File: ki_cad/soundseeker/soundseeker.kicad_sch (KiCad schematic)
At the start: 0 parts

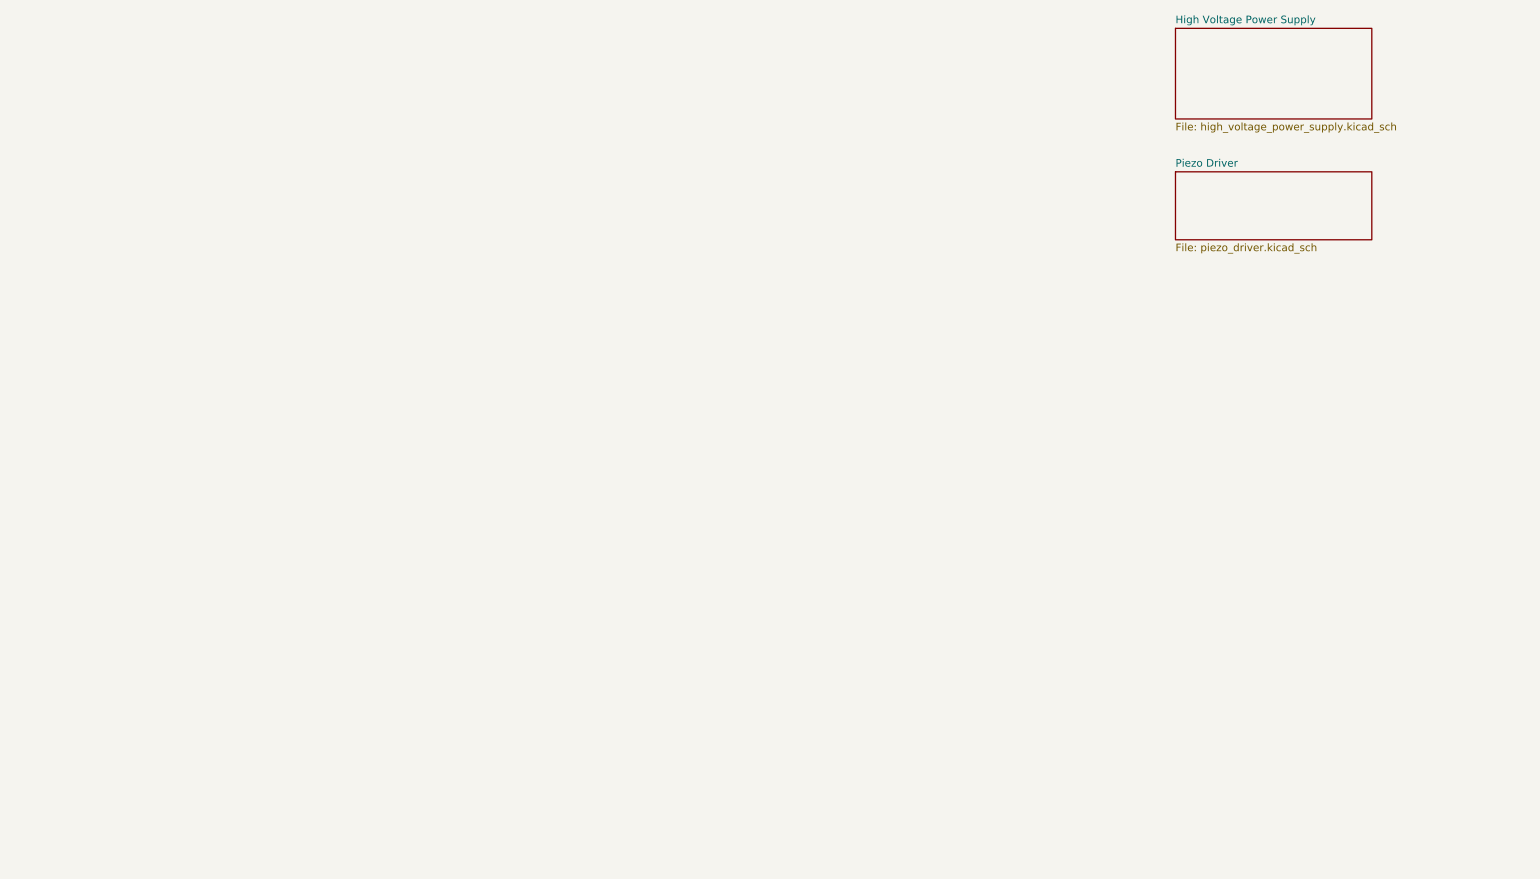
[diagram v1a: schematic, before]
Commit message: add preamp schematic
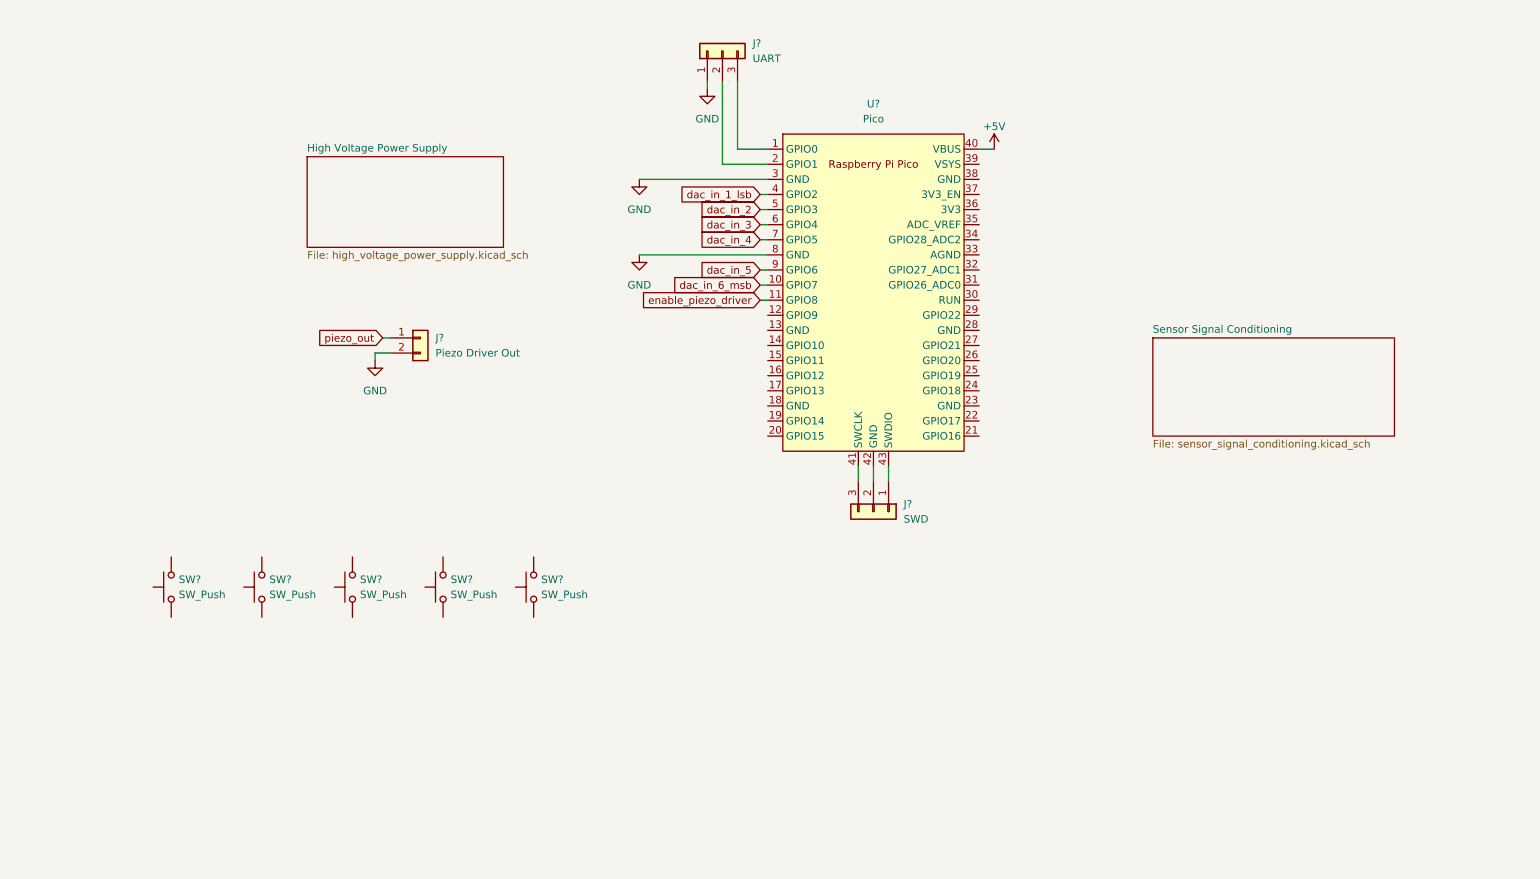
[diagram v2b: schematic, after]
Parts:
- added J?: SWD, symbol Connector_Generic:Conn_01x03
- added J?: Piezo Driver Out, symbol Connector_Generic:Conn_01x02
- added J?: UART, symbol Connector_Generic:Conn_01x03
- added SW? (x5): SW_Push, symbol Switch:SW_Push
- added U?: Pico, RPi_Pico:RPi_Pico_SMD_TH, symbol MCU_RaspberryPi_and_Boards:Pico
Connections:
- new net: J?.1 (Pin_1), U?.43 (SWDIO)
- new net: J?.2 (Pin_2), U?.42 (GND)
- new net: J?.3 (Pin_3), U?.41 (SWCLK)
- new net: J?.2 (Pin_2), U?.2 (GPIO1)
- new net: J?.3 (Pin_3), U?.1 (GPIO0)
- new net +5V: U?.40 (VBUS)
- new net GND: J?.1 (Pin_1), J?.2 (Pin_2), U?.3 (GND), U?.8 (GND)
- new net dac_in_1_lsb: U?.4 (GPIO2)
- new net dac_in_2: U?.5 (GPIO3)
- new net dac_in_3: U?.6 (GPIO4)
- new net dac_in_4: U?.7 (GPIO5)
- new net dac_in_5: U?.9 (GPIO6)
- new net dac_in_6_msb: U?.10 (GPIO7)
- new net enable_piezo_driver: U?.11 (GPIO8)
- new net piezo_out: J?.1 (Pin_1)
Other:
- removed sheet Piezo Driver
- added sheet Sensor Signal Conditioning (sensor_signal_conditioning.kicad_sch)

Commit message: schematic
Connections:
- net GND: now also U?.13 (GND), U?.18 (GND), U?.23 (GND), U?.28 (GND), U?.38 (GND)
- net ADC_DOUT: now reaches U?.21 (GPIO16)
- net ADC_CS: now reaches U?.22 (GPIO17)
- net ADC_SLCK: now reaches U?.24 (GPIO18)
- net enable_analog_power_supply: now reaches U?.26 (GPIO20)

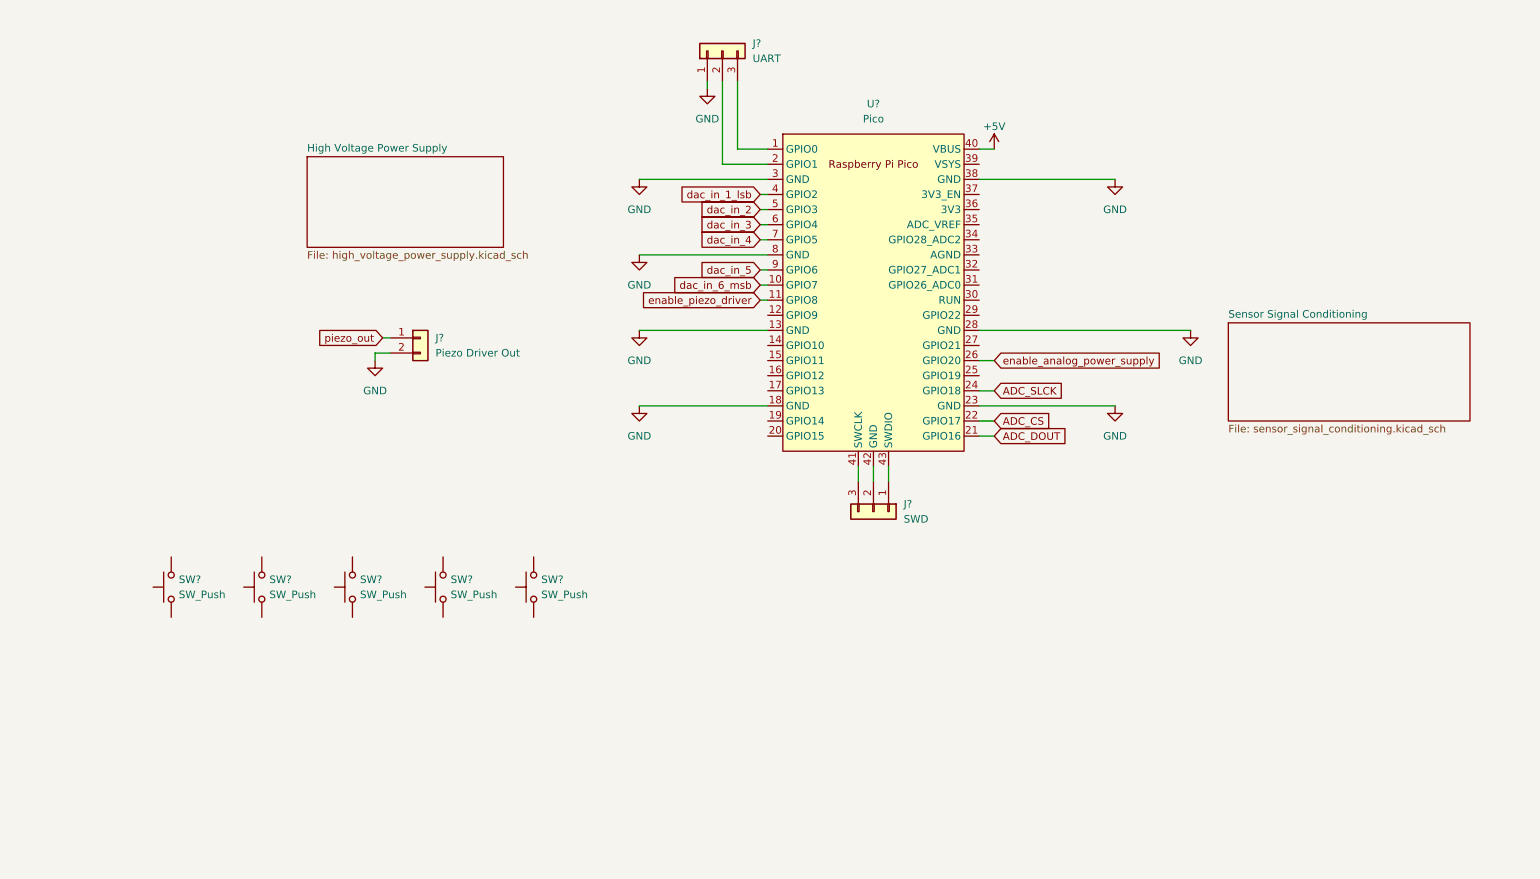
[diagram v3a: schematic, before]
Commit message: add buttons and display spi connections
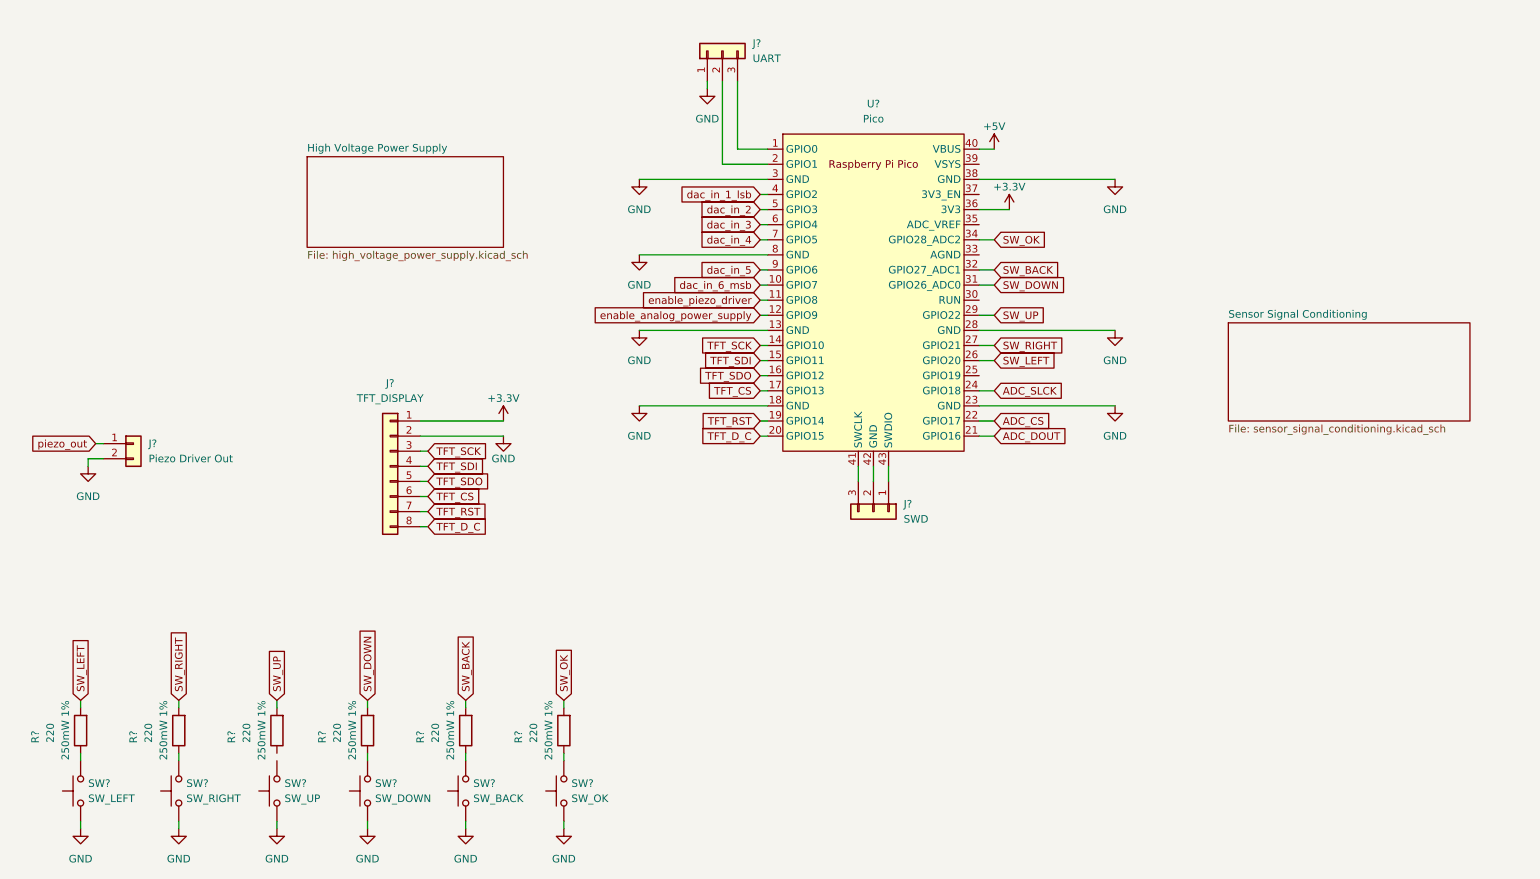
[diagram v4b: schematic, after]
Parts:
- removed SW?: SW_Push, symbol Switch:SW_Push
- added J?: TFT_DISPLAY, symbol Connector_Generic:Conn_01x08
- added R? (x6): 220, Resistor_SMD:R_0805_2012Metric_Pad1.20x1.40mm_HandSolder, symbol Device:R
- added SW?: SW_BACK, symbol Switch:SW_Push
- added SW?: SW_OK, symbol Switch:SW_Push
- SW?: value SW_Push -> SW_DOWN
- SW?: value SW_Push -> SW_RIGHT
- SW?: value SW_Push -> SW_LEFT
- SW?: value SW_Push -> SW_UP
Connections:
- net GND: now also SW?.1, SW?.1, SW?.1, SW?.1, J?.2 (Pin_2), SW?.1, SW?.1
- net enable_analog_power_supply: now also U?.12 (GPIO9); no longer U?.26 (GPIO20)
- net at SW?.2: now also R?.1 (x3)
- net TFT_SCK: now reaches U?.14 (GPIO10)
- net TFT_SCK: now also J?.3 (Pin_3)
- net TFT_SDI: now reaches U?.15 (GPIO11)
- net TFT_SDI: now also J?.4 (Pin_4)
- net TFT_SDO: now reaches U?.16 (GPIO12)
- net TFT_SDO: now also J?.5 (Pin_5)
- net TFT_CS: now reaches U?.17 (GPIO13)
- net TFT_CS: now also J?.6 (Pin_6)
- net TFT_RST: now reaches U?.19 (GPIO14)
- net TFT_RST: now also J?.7 (Pin_7)
- net TFT_D_C: now reaches U?.20 (GPIO15)
- net TFT_D_C: now also J?.8 (Pin_8)
- net SW_RIGHT: now reaches U?.27 (GPIO21)
- net SW_RIGHT: now also R?.2
- net SW_UP: now reaches U?.29 (GPIO22)
- net SW_UP: now also R?.2
- net SW_DOWN: now reaches U?.31 (GPIO26_ADC0)
- net SW_DOWN: now also R?.2
- net SW_BACK: now reaches U?.32 (GPIO27_ADC1)
- net SW_BACK: now also R?.2
- net SW_OK: now reaches U?.34 (GPIO28_ADC2)
- net SW_OK: now also R?.2
- net +3.3V: now reaches U?.36 (3V3)
- net +3.3V: now also J?.1 (Pin_1)
- new net: R?.1, SW?.2 (x2)
- new net SW_LEFT: R?.2, U?.26 (GPIO20)
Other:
- moved on the sheet: J?, SW?

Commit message: sounseeker base board (evaluartion) PCB layout
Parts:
- removed J?: Piezo Driver Out, symbol Connector_Generic:Conn_01x02
- J2: renamed from J?; footprint (none) -> Connector_PinHeader_2.54mm:PinHeader_1x08_P2.54mm_Vertical
- J3, J4: renamed from J?; footprint (none) -> Connector_PinHeader_2.54mm:PinHeader_1x03_P2.54mm_Vertical
- SW1, SW2, SW3, SW4, SW5, SW6: renamed from SW?; footprint (none) -> Button_Switch_THT:SW_PUSH_6mm
- U2: renamed from U?; footprint RPi_Pico:RPi_Pico_SMD_TH -> MCU_RaspberryPi_and_Boards:RPi_Pico_SMD_TH
- gave numbers to parts that had none: 6
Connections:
- net SW_DOWN: now also U2.29 (GPIO22); no longer U2.31 (GPIO26_ADC0)
- net SW_RIGHT: now also U2.31 (GPIO26_ADC0); no longer U2.27 (GPIO21)
- net SW_UP: now also U2.27 (GPIO21); no longer U2.29 (GPIO22)
- net at R18.1: now also SW3.2

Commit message: finish base board (evaluation)
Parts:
- J2: value TFT_DISPLAY -> 1x08
- J3: value UART -> 1x03; description (none) -> UART
- J4: value SWD -> 1x03; description (none) -> SWD
- SW1: value SW_LEFT -> SW; description (none) -> LEFT
- SW2: value SW_RIGHT -> SW; description (none) -> RIGHT
- SW3: value SW_UP -> SW; description (none) -> UP
- SW4: value SW_DOWN -> SW; description (none) -> DOWN
- SW5: value SW_BACK -> SW; description (none) -> BACK
- SW6: value SW_OK -> SW; description (none) -> OK
